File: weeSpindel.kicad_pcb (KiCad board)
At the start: 2 copper layers, 105.9 x 17.8 mm, 22 parts, among them J1 MPU-6050, SW1 POWER, U1 ESP-12E, U2 HT7733SA, U3 MCP1700-3302E_SOT23

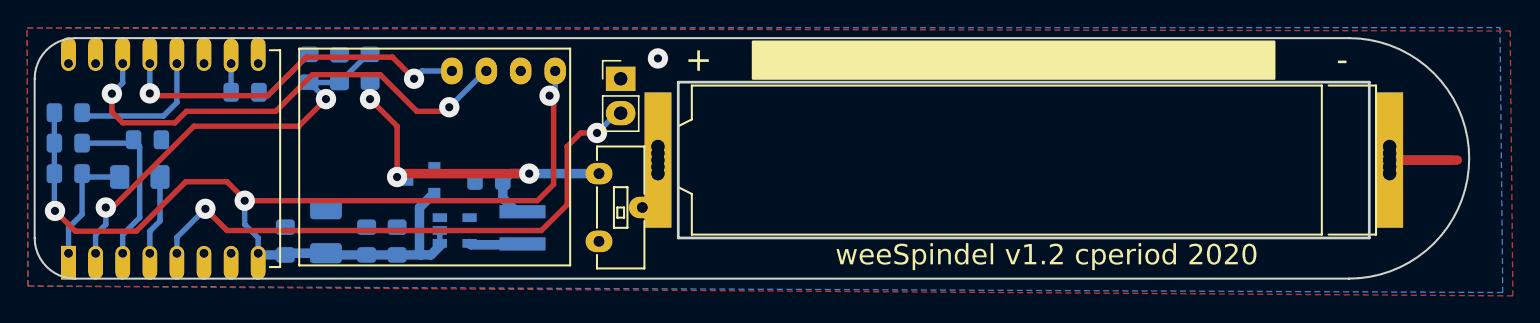
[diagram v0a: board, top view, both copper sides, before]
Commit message: simpler, shorter version that uses lipo battery pack with JST-PH2.0 connectors
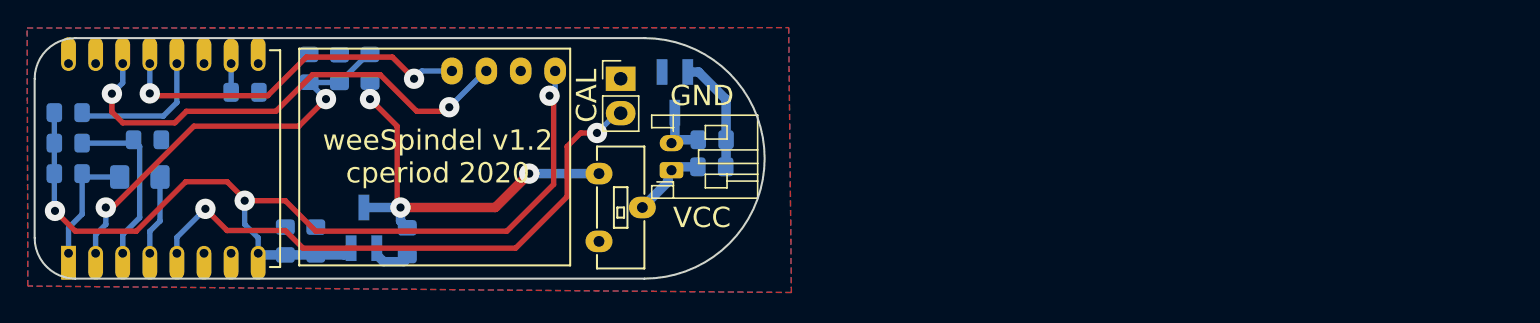
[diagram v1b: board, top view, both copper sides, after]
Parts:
- removed C5: 100uF, Capacitor_Tantalum_SMD:CP_EIA-3528-12_Kemet-T_Pad1.50x2.35mm_HandSolder
- removed L1: 10uH, Inductor_SMD:L_Coilcraft_XxL4040
- added R8: 100R, Resistor_SMD:R_0805_2012Metric_Pad1.15x1.40mm_HandSolder, B.Cu at (141.0, 105.5)
- BT1: value NiMH -> Li 3.7v; footprint CPB:Battery_Springs_AAA -> Connector_JST:JST_PH_S2B-PH-K_1x02_P2.00mm_Horizontal
- C3: value 10uF -> 22uF
- C4: value 10uF -> 100nF
- U2: value HT7733SA -> BRCL3130MC; footprint Package_TO_SOT_SMD:SOT-23-5 -> Package_TO_SOT_SMD:SOT-23_Handsoldering
- U3: value MCP1700-3302E_SOT23 -> HT7333; footprint Package_TO_SOT_SMD:SOT-23 -> Package_TO_SOT_SMD:SOT-23_Handsoldering
- moved C4 26.6 mm to (141.0, 103.5), turned to 180 degrees
- moved BT1 26.0 mm to (138.0, 105.8), turned to 90 degrees
- moved U2 19.2 mm to (138.2, 100.0), turned to 270 degrees
- moved C2 7.54 mm to (118.5, 111.0), turned to 270 degrees
- moved C3 6.00 mm to (111.8, 111.0)
- moved U3 5.47 mm to (115.3, 110.0), turned to 90 degrees
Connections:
- BT1 pad 2: GND -> Net-(BT1-Pad2)
- C4 pad 1: 3V3 -> Net-(C4-Pad1)
- C4 pad 2: GND -> Net-(BT1-Pad2)
- U2 pad 1: 3V3 -> GND
- U2 pad 2: 3V3 -> Net-(C4-Pad1)
- U2 pad 3: Net-(U2-Pad3) -> Net-(BT1-Pad2)
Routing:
- net 3V3: track 80.3 -> 69.5 mm
- net Net-(C4-Pad1): track 0.00 -> 8.60 mm
- net GND: track 9.71 -> 3.31 mm, vias 1 -> 0
- net Net-(BT1-Pad2): track 0.00 -> 3.72 mm
- net Net-(L1-Pad2): track 3.38 -> 0.00 mm
- net Net-(BT1-Pad1): track 4.18 -> 5.99 mm
- net Net-(C2-Pad1): track 29.0 -> 30.3 mm
- net Net-(JP1-Pad2): track 41.6 -> 42.3 mm
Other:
- board size 105.9 x 17.8 mm -> 53.9 x 17.8 mm
- board text added: "CAL"
- board text added: "GND"
- board text added: "VCC"
- board text removed: "+"
- board text removed: "-"

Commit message: progress on a smaller version using a JST-PH lipo cell off the end
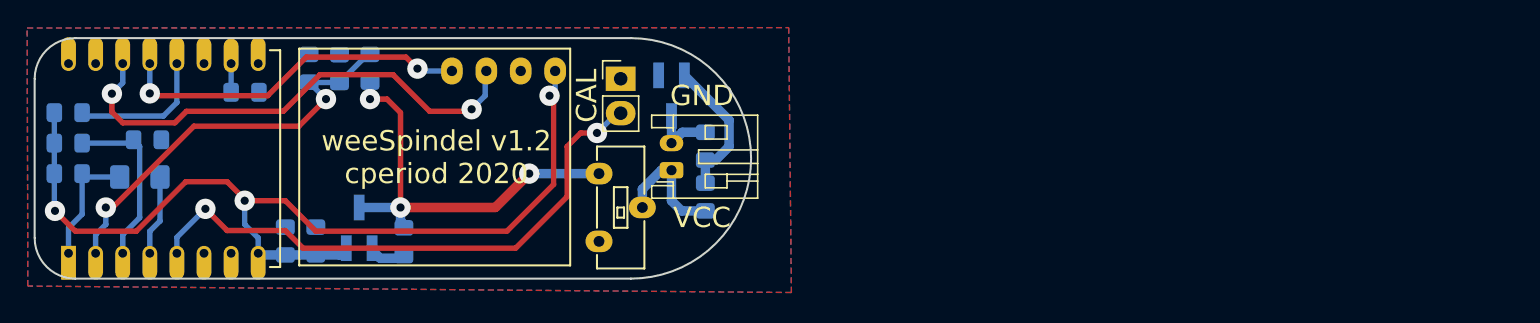
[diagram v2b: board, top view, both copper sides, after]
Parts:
- moved R8 2.28 mm to (140.5, 107.7), turned to 270 degrees
- moved C4 0.69 mm to (140.5, 104.0), turned to 90 degrees
- moved U2 0.35 mm to (138.0, 100.2)
- moved U3 0.35 mm to (115.0, 110.0)
- moved C2 0.25 mm to (118.2, 111.0)
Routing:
- net Net-(BT1-Pad1): track 5.99 -> 9.14 mm
- net Net-(C4-Pad1): track 8.60 -> 10.5 mm
- net SCL: track 35.7 -> 36.8 mm
- net Net-(C2-Pad1): track 30.3 -> 31.3 mm
- net Net-(BT1-Pad2): track 3.72 -> 4.68 mm
- net GND: track 3.31 -> 2.71 mm
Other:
- board size 53.9 x 17.8 mm -> 52.9 x 17.8 mm

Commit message: add USB programming
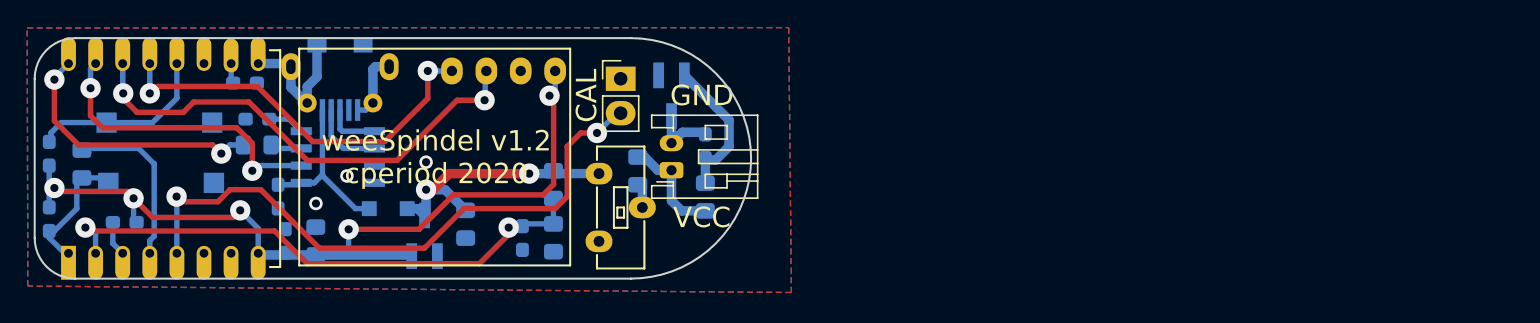
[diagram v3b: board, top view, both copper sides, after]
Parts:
- removed C7: 100nF, Capacitor_SMD:C_0805_2012Metric_Pad1.15x1.40mm_HandSolder
- added C5: 100nF, Capacitor_SMD:C_0603_1608Metric_Pad1.05x0.95mm_HandSolder, B.Cu at (107.4, 102.0)
- added C8: 100nF, Capacitor_SMD:C_0603_1608Metric_Pad1.05x0.95mm_HandSolder, B.Cu at (109.0, 107.7)
- added D1: B5817WL, Diode_SMD:D_SOD-123F, B.Cu at (117.1, 108.6)
- added F1: 350mA, Fuse:Fuse_0805_2012Metric_Pad1.15x1.40mm_HandSolder, B.Cu at (135.5, 105.8)
- added J2: USB_B_Micro, CPB:USB Micro-B C10418, B.Cu at (113.5, 102.1)
- added R9: 470R, Resistor_SMD:R_0805_2012Metric_Pad1.15x1.40mm_HandSolder, B.Cu at (107.4, 103.9)
- added SW2: RESET, Button_Switch_SMD:SW_SPST_CK_RS282G05A3, B.Cu at (100.3, 106.7)
- added SW3: PROG, Button_Switch_SMD:SW_SPST_CK_RS282G05A3, B.Cu at (100.2, 102.2)
- added U4: CH330N, Package_SO:SOIC-8_3.9x4.9mm_P1.27mm, B.Cu at (113.4, 104.8)
- C1, C4, C6: footprint Capacitor_SMD:C_0805_2012Metric_Pad1.15x1.40mm_HandSolder -> Capacitor_SMD:C_0603_1608Metric_Pad1.05x0.95mm_HandSolder
- R3: footprint Resistor_SMD:R_1206_3216Metric_Pad1.42x1.75mm_HandSolder -> Resistor_SMD:R_0805_2012Metric_Pad1.15x1.40mm_HandSolder
- R4, R5, R6, R7: footprint Resistor_SMD:R_0805_2012Metric_Pad1.15x1.40mm_HandSolder -> Resistor_SMD:R_0603_1608Metric_Pad1.05x0.95mm_HandSolder
- U3: value HT7333 -> HT7233
- moved R2 20.1 mm to (129.3, 110.7), turned to 90 degrees
- moved C6 20.1 mm to (127.0, 110.8), turned to 270 degrees
- moved R1 16.0 mm to (129.3, 106.8), turned to 90 degrees
- moved R6 7.19 mm to (97.6, 109.6), turned to 0 degrees
- moved U3 4.86 mm to (119.8, 110.6)
- moved C2 4.74 mm to (122.8, 109.7)
- moved R3 4.38 mm to (94.5, 105.3), turned to 270 degrees
- moved R5 3.64 mm to (92.1, 109.4), turned to 90 degrees
- moved R4 3.34 mm to (92.1, 104.5), turned to 270 degrees
- moved R7 0.69 mm to (106.5, 99.3)
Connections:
- net Net-(C2-Pad1) renamed +5V
- SW1 pad 2: Net-(BT1-Pad1) -> Net-(F1-Pad1)
- U1 pad 15: Net-(U1-Pad15) -> eRX
- U1 pad 16: Net-(U1-Pad16) -> eTX
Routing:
- net eRX: track 0.00 -> 22.6 mm, vias 0 -> 2
- net eTX: track 0.00 -> 19.9 mm, vias 0 -> 2
- net Net-(C8-Pad1): track 0.00 -> 12.9 mm
- net GND: track 2.71 -> 14.9 mm, vias 0 -> 3
- net +5V: track 31.3 -> 20.2 mm, vias 3 -> 2
- net ADC: track 30.4 -> 41.4 mm
- net Net-(R6-Pad1): track 12.7 -> 2.63 mm
- net Net-(R3-Pad1): track 5.94 -> 12.5 mm
- net Net-(J2-Pad2): track 0.00 -> 5.49 mm
- net Net-(J2-Pad3): track 0.00 -> 4.01 mm
- net 3V3: track 69.1 -> 65.5 mm, vias 3 -> 5
- net SDA: track 26.2 -> 29.7 mm
- net Net-(JP1-Pad2): track 42.3 -> 45.6 mm
- net Net-(R4-Pad1): track 10.4 -> 13.5 mm
- net Net-(C5-Pad1): track 0.00 -> 2.73 mm
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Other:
- net class Default: clearance 0.6 -> 0.4
- rule trace_clearance: 0.6 -> 0.4
- rule via_min_size: 1.5 -> 1
- board text added: "BATTERY OFF BEFORE USB"
- board text added: "PRG"
- board text added: "RST"

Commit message: a bit of tidying up to make it easier to mill and assemble
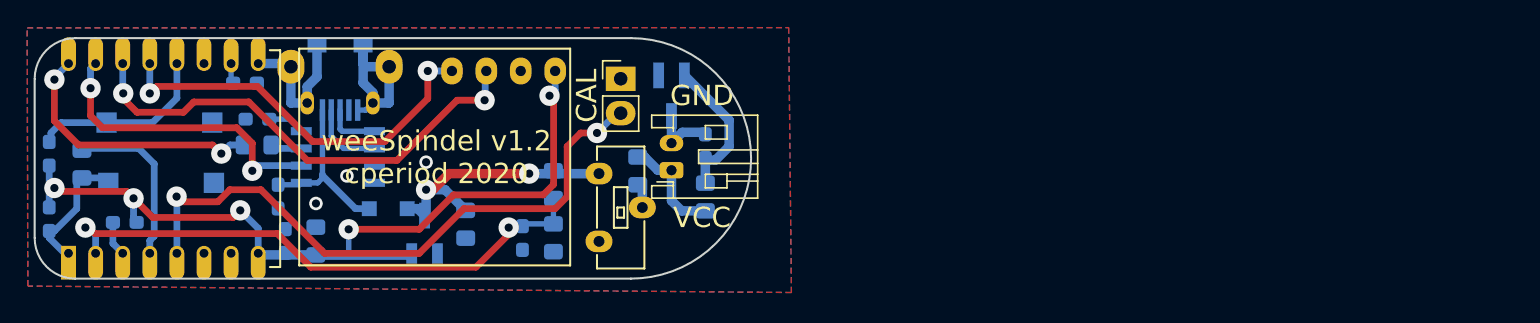
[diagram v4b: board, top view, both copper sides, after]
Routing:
- net GND: track 14.9 -> 23.2 mm

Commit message: more tidying
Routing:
- net 3V3: track 65.5 -> 61.1 mm
- net +5V: track 20.2 -> 21.4 mm
- net GND: vias 3 -> 7
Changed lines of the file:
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@@
     (thickness 1.6)
     (drawings 13)
-    (tracks 216)
+    (tracks 219)
     (zones 0)
     (modules 29)
@@
   )
   (setup
-    (last_trace_width 0.7)
+    (last_trace_width 0.5)
     (user_trace_width 0.5)
     (user_trace_width 0.7)
@@
   (via (at 111.76 108.204) (size 1) (drill 0.6) (layers F.Cu B.Cu) (net 1))
   (via (at 114.046 106.172) (size 1) (drill 0.6) (layers F.Cu B.Cu) (net 1))
-  (via (at 119.888 105.156) (size 1) (drill 0.6) (layers F.Cu B.Cu) (net 1))
   (segment (start 109.684 97.879) (end 109.913 98.108) (width 0.7) (layer B.Cu) (net 1))
   (segment (start 107.497 97.879) (end 109.684 97.879) (width 0.7) (layer B.Cu) (net 1))
@@
   (segment (start 115.238 99.2995) (end 115.238 96.82501) (width 0.7) (layer B.Cu) (net 1))
   (segment (start 115.963 100.0245) (end 115.238 99.2995) (width 0.7) (layer B.Cu) (net 1))
-  (segment (start 129.413 99.837) (end 129.413 98.425) (width 0.5) (layer B.Cu) (net 2) (status 20))
-  (segment (start 121.92 107.569) (end 128.531 107.569) (width 0.5) (layer F.Cu) (net 2))
-  (segment (start 119.38 110.109) (end 121.92 107.569) (width 0.5) (layer F.Cu) (net 2))
-  (segment (start 128.531 107.569) (end 129.3 106.8) (width 0.5) (layer F.Cu) (net 2))
-  (via (at 114.173 110.109) (size 1.5) (drill 0.6) (layers F.Cu B.Cu) (net 2))
-  (segment (start 129.3 106.8) (end 129.3 100.55) (width 0.5) (layer F.Cu) (net 2))
-  (segment (start 129.3 100.55) (end 129 100.25) (width 0.5) (layer F.Cu) (net 2))
-  (segment (start 113.792 110.109) (end 119.38 110.109) (width 0.5) (layer F.Cu) (net 2))
-  (segment (start 129 100.25) (end 129.413 99.837) (width 0.5) (layer B.Cu) (net 2))
-  (via (at 129 100.25) (size 1.5) (drill 0.6) (layers F.Cu B.Cu) (net 2))
+  (via (at 132.5245 108.5215) (size 1) (drill 0.6) (layers F.Cu B.Cu) (net 1))
+  (via (at 125.5395 112.649) (size 1) (drill 0.6) (layers F.Cu B.Cu) (net 1))
+  (via (at 129.032 102.8065) (size 1) (drill 0.6) (layers F.Cu B.Cu) (net 1))
+  (via (at 116.586 110.363) (size 1) (drill 0.6) (layers F.Cu B.Cu) (net 1))
+  (via (at 125.857 106.934) (size 1) (drill 0.6) (layers F.Cu B.Cu) (net 1))
   (segment (start 109.625 111.875) (end 109.5 112) (width 0.7) (layer B.Cu) (net 2) (status 30))
   (segment (start 107.618 112) (end 107.497 111.879) (width 0.7) (layer B.Cu) (net 2) (status 30))
@@
   (segment (start 114.046 112.014) (end 111.887 112.014) (width 0.4) (layer B.Cu) (net 2))
   (segment (start 114.173 111.887) (end 114.046 112.014) (width 0.4) (layer B.Cu) (net 2))
+  (via (at 114.173 110.109) (size 1.5) (drill 0.6) (layers F.Cu B.Cu) (net 2))
+  (segment (start 114.173 110.109) (end 114.4905 110.109) (width 0.5) (layer F.Cu) (net 2))
+  (segment (start 114.4905 110.109) (end 121.9835 102.616) (width 0.5) (layer F.Cu) (net 2))
+  (via (at 129.0955 100.584) (size 1.5) (drill 0.6) (layers F.Cu B.Cu) (net 2))
+  (segment (start 121.9835 102.616) (end 127.0635 102.616) (width 0.5) (layer F.Cu) (net 2))
+  (segment (start 127.0635 102.616) (end 129.0955 100.584) (width 0.5) (layer F.Cu) (net 2))
+  (segment (start 129.413 100.2665) (end 129.413 98.425) (width 0.5) (layer B.Cu) (net 2))
+  (segment (start 129.0955 100.584) (end 129.413 100.2665) (width 0.5) (layer B.Cu) (net 2))
   (segment (start 129.286 107.841) (end 129.286 109.71) (width 0.4) (layer B.Cu) (net 3))
   (segment (start 127.018 109.71) (end 127 109.728) (width 0.4) (layer B.Cu) (net 3))
@@
   (segment (start 108.9025 110.4265) (end 95.4405 110.4265) (width 0.5) (layer F.Cu) (net 3))
   (segment (start 111.379 112.903) (end 108.9025 110.4265) (width 0.5) (layer F.Cu) (net 3))
-  (segment (start 123.571 112.903) (end 111.379 112.903) (width 0.5) (layer F.Cu) (net 3))
-  (segment (start 125.984 109.982) (end 125.984 110.49) (width 0.5) (layer F.Cu) (net 3))
-  (segment (start 125.984 110.49) (end 123.571 112.903) (width 0.5) (layer F.Cu) (net 3))
+  (segment (start 122.8725 112.903) (end 111.379 112.903) (width 0.5) (layer F.Cu) (net 3))
+  (segment (start 125.984 109.982) (end 125.7935 109.982) (width 0.5) (layer F.Cu) (net 3))
+  (segment (start 125.7935 109.982) (end 122.8725 112.903) (width 0.5) (layer F.Cu) (net 3))
   (segment (start 124.41 97.99) (end 124.42 98) (width 0.4) (layer B.Cu) (net 4) (status 30))
   (via (at 124.206 100.584) (size 1.5) (drill 0.6) (layers F.Cu B.Cu) (net 4))
@@
   (segment (start 99.497 97.879) (end 99.497 100.079) (width 0.5) (layer B.Cu) (net 5) (status 10))
   (segment (start 132.5 103) (end 133.96 101.54) (width 0.5) (layer B.Cu) (net 6) (status 20))
-  (segment (start 107.696 107.188) (end 112.395 111.887) (width 0.5) (layer F.Cu) (net 6))
-  (segment (start 112.395 111.887) (end 119.38 111.887) (width 0.5) (layer F.Cu) (net 6))
-  (segment (start 105.41 107.188) (end 107.696 107.188) (width 0.5) (layer F.Cu) (net 6))
-  (segment (start 101.473 107.696) (end 101.854 108.077) (width 0.5) (layer F.Cu) (net 6))
-  (segment (start 104.521 108.077) (end 105.41 107.188) (width 0.5) (layer F.Cu) (net 6))
-  (segment (start 101.854 108.077) (end 104.521 108.077) (width 0.5) (layer F.Cu) (net 6))
-  (segment (start 130.3 104) (end 131.3 103) (width 0.5) (layer F.Cu) (net 6))
-  (segment (start 119.38 111.887) (end 122.682 108.585) (width 0.5) (layer F.Cu) (net 6))
-  (segment (start 122.682 108.585) (end 129.415 108.585) (width 0.5) (layer F.Cu) (net 6))
-  (segment (start 129.415 108.585) (end 130.3 107.7) (width 0.5) (layer F.Cu) (net 6))
-  (segment (start 130.3 107.7) (end 130.3 104) (width 0.5) (layer F.Cu) (net 6))
-  (segment (start 131.3 103) (end 132.5 103) (width 0.5) (layer F.Cu) (net 6))
   (via (at 132.5 103) (size 1.5) (drill 0.6) (layers F.Cu B.Cu) (net 6))
   (segment (start 133.96 101.54) (end 134.25 101.54) (width 0.5) (layer B.Cu) (net 6) (status 30))
@@
   (segment (start 101.497 107.72) (end 101.497 111.879) (width 0.5) (layer B.Cu) (net 6))
   (segment (start 101.473 107.696) (end 101.497 107.72) (width 0.5) (layer B.Cu) (net 6))
+  (segment (start 130.3 107.7) (end 130.3 104) (width 0.5) (layer F.Cu) (net 6))
+  (segment (start 129.4785 108.5215) (end 130.3 107.7) (width 0.5) (layer F.Cu) (net 6))
+  (segment (start 125.349 108.5215) (end 129.4785 108.5215) (width 0.5) (layer F.Cu) (net 6))
+  (segment (start 101.854 108.077) (end 104.521 108.077) (width 0.5) (layer F.Cu) (net 6))
+  (segment (start 130.3 104) (end 131.3 103) (width 0.5) (layer F.Cu) (net 6))
+  (segment (start 105.41 107.188) (end 107.696 107.188) (width 0.5) (layer F.Cu) (net 6))
+  (segment (start 131.3 103) (end 132.5 103) (width 0.5) (layer F.Cu) (net 6))
+  (segment (start 121.9835 111.887) (end 125.349 108.5215) (width 0.5) (layer F.Cu) (net 6))
+  (segment (start 101.473 107.696) (end 101.854 108.077) (width 0.5) (layer F.Cu) (net 6))
+  (segment (start 104.521 108.077) (end 105.41 107.188) (width 0.5) (layer F.Cu) (net 6))
+  (segment (start 112.395 111.887) (end 121.9835 111.887) (width 0.5) (layer F.Cu) (net 6))
+  (segment (start 107.696 107.188) (end 112.395 111.887) (width 0.5) (layer F.Cu) (net 6))
   (segment (start 138 105.75) (end 138 108) (width 0.7) (layer B.Cu) (net 7))
   (segment (start 138.75 108.75) (end 140.5 108.75) (width 0.7) (layer B.Cu) (net 7))
@@
   (segment (start 108.712 104.14) (end 108.458 103.886) (width 0.5) (layer B.Cu) (net 19))
   (segment (start 110.678 104.14) (end 108.712 104.14) (width 0.5) (layer B.Cu) (net 19))
-  (via (at 127.5 106) (size 1.5) (drill 0.6) (layers F.Cu B.Cu) (net 20))
-  (segment (start 127.5 106) (end 131.9 106) (width 0.7) (layer B.Cu) (net 20) (status 20))
-  (segment (start 131.9 106) (end 132.65 106) (width 0.7) (layer B.Cu) (net 20) (status 30))
-  (segment (start 119.888 107.188) (end 120.396 107.188) (width 0.7) (layer F.Cu) (net 20))
-  (segment (start 121.584 106) (end 127.5 106) (width 0.7) (layer F.Cu) (net 20))
   (via (at 119.888 107.188) (size 1.5) (drill 0.6) (layers F.Cu B.Cu) (net 20))
-  (segment (start 120.396 107.188) (end 121.584 106) (width 0.7) (layer F.Cu) (net 20))
   (segment (start 119.888 107.188) (end 119.888 109.093) (width 0.7) (layer B.Cu) (net 20))
   (segment (start 121.285 107.188) (end 122.809 108.712) (width 0.7) (layer B.Cu) (net 20))
@@
   (segment (start 119.268 108.585) (end 119.776 109.093) (width 0.7) (layer B.Cu) (net 20))
   (segment (start 118.494 108.585) (end 119.268 108.585) (width 0.7) (layer B.Cu) (net 20))
+  (segment (start 120.396 107.188) (end 119.888 107.188) (width 0.7) (layer F.Cu) (net 20))
+  (via (at 126.3015 104.521) (size 1.5) (drill 0.6) (layers F.Cu B.Cu) (net 20))
+  (segment (start 126.3015 104.521) (end 123.063 104.521) (width 0.7) (layer F.Cu) (net 20))
+  (segment (start 123.063 104.521) (end 120.396 107.188) (width 0.7) (layer F.Cu) (net 20))
+  (segment (start 132.187 105.537) (end 132.65 106) (width 0.7) (layer B.Cu) (net 20))
+  (segment (start 126.3015 104.521) (end 127.3175 105.537) (width 0.7) (layer B.Cu) (net 20))
+  (segment (start 127.3175 105.537) (end 132.187 105.537) (width 0.7) (layer B.Cu) (net 20))
   (segment (start 113.538 101.308) (end 113.538 102.718) (width 0.4) (layer B.Cu) (net 21))
   (segment (start 113.69 102.87) (end 116.078 102.87) (width 0.4) (layer B.Cu) (net 21))
